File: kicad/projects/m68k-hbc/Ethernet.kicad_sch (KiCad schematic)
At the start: 19 parts, among them J17 RJ45_Amphenol_RJMG1BD3B8K1ANR, U29 RTL8019AS, Y7 20M

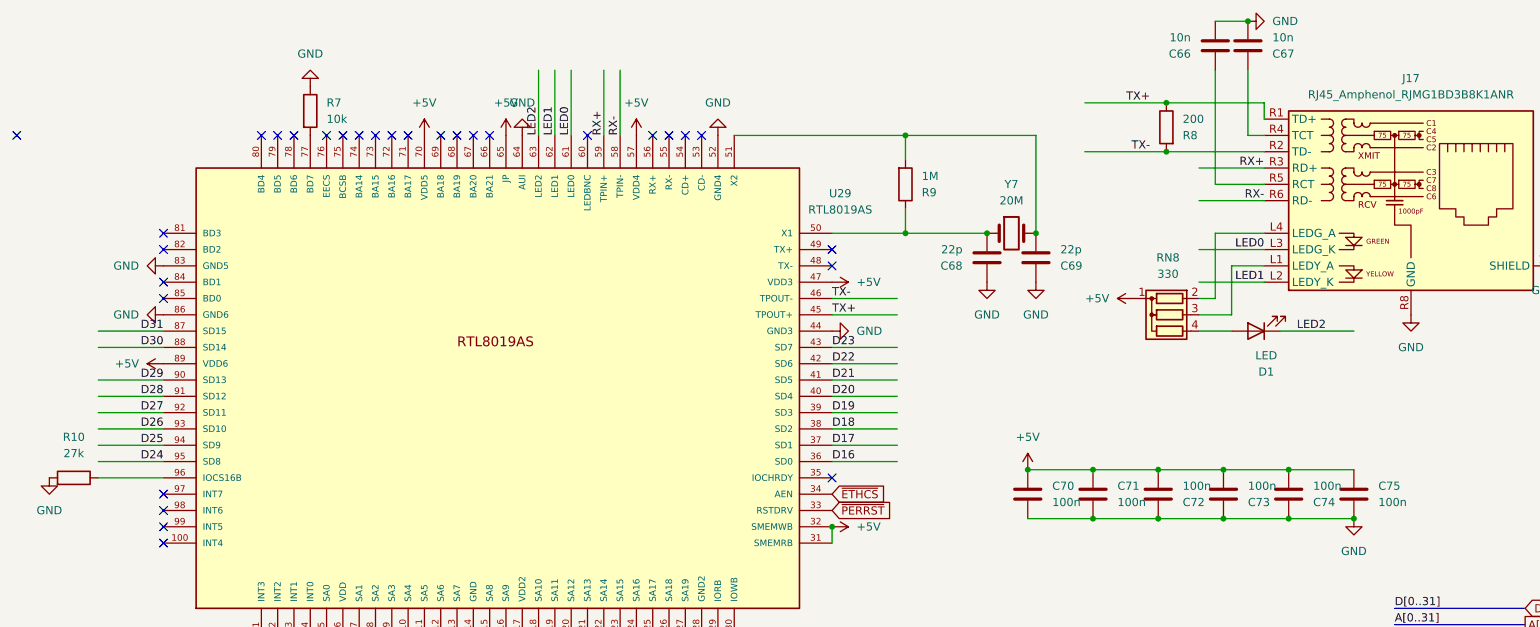
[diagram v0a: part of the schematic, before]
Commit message: Modified system architecture, New KiCad Project: Cache Memory Module(SIMM80)
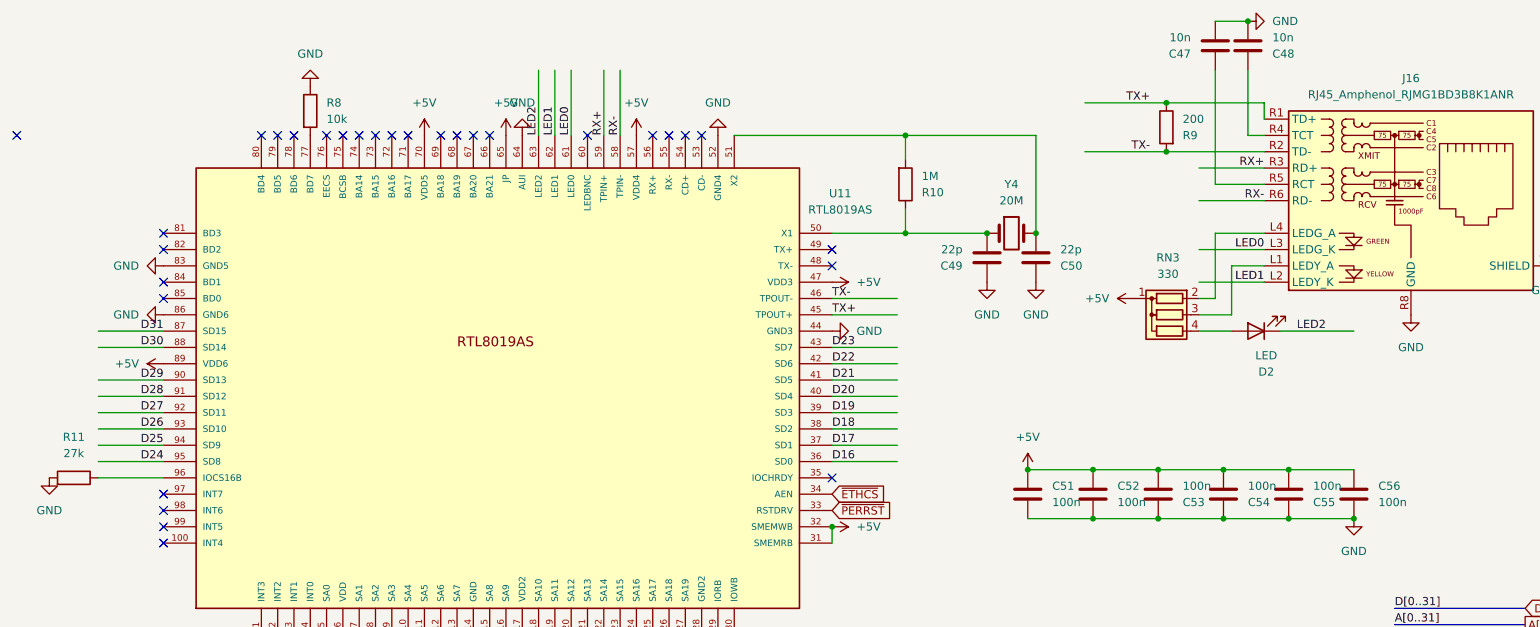
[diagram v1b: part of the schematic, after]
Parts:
- renumbered C66 to C47, C67 to C48, C68 to C49, C69 to C50, C70 to C51, C71 to C52, C72 to C53, C73 to C54, C74 to C55, C75 to C56, D1 to D2, J17 to J16, R9 to R10, R10 to R11, R7 to R8, R8 to R9, RN8 to RN3, U29 to U11, Y7 to Y4

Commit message: Some Updates
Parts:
- removed R11: 27k, Resistor_SMD:R_1206_3216Metric_Pad1.30x1.75mm_HandSolder, symbol Device:R
- removed R8: 10k, Resistor_SMD:R_1206_3216Metric_Pad1.30x1.75mm_HandSolder, symbol Device:R
- C67: renamed from C47; value 10n -> C; footprint Capacitor_SMD:C_1206_3216Metric_Pad1.33x1.80mm_HandSolder -> Capacitor_SMD:C_0603_1608Metric_Pad1.08x0.95mm_HandSolder
- C68: renamed from C48; value 10n -> C; footprint Capacitor_SMD:C_1206_3216Metric_Pad1.33x1.80mm_HandSolder -> Capacitor_SMD:C_0603_1608Metric_Pad1.08x0.95mm_HandSolder
- C69: renamed from C49; value 22p -> C; footprint Capacitor_SMD:C_1206_3216Metric_Pad1.33x1.80mm_HandSolder -> Capacitor_SMD:C_0603_1608Metric_Pad1.08x0.95mm_HandSolder
- C70: renamed from C50; value 22p -> C; footprint Capacitor_SMD:C_1206_3216Metric_Pad1.33x1.80mm_HandSolder -> Capacitor_SMD:C_0603_1608Metric_Pad1.08x0.95mm_HandSolder
- C71: renamed from C51; value 100n -> C; footprint Capacitor_SMD:C_1206_3216Metric_Pad1.33x1.80mm_HandSolder -> Capacitor_SMD:C_0603_1608Metric_Pad1.08x0.95mm_HandSolder
- C72: renamed from C52; value 100n -> C; footprint Capacitor_SMD:C_1206_3216Metric_Pad1.33x1.80mm_HandSolder -> Capacitor_SMD:C_0603_1608Metric_Pad1.08x0.95mm_HandSolder
- C73: renamed from C53; value 100n -> C; footprint Capacitor_SMD:C_1206_3216Metric_Pad1.33x1.80mm_HandSolder -> Capacitor_SMD:C_0603_1608Metric_Pad1.08x0.95mm_HandSolder
- C74: renamed from C54; value 100n -> C; footprint Capacitor_SMD:C_1206_3216Metric_Pad1.33x1.80mm_HandSolder -> Capacitor_SMD:C_0603_1608Metric_Pad1.08x0.95mm_HandSolder
- C75: renamed from C55; value 100n -> C; footprint Capacitor_SMD:C_1206_3216Metric_Pad1.33x1.80mm_HandSolder -> Capacitor_SMD:C_0603_1608Metric_Pad1.08x0.95mm_HandSolder
- C76: renamed from C56; value 100n -> C; footprint Capacitor_SMD:C_1206_3216Metric_Pad1.33x1.80mm_HandSolder -> Capacitor_SMD:C_0603_1608Metric_Pad1.08x0.95mm_HandSolder
- R6: renamed from R9; value 200 -> R; footprint Resistor_SMD:R_1206_3216Metric_Pad1.30x1.75mm_HandSolder -> Resistor_SMD:R_0603_1608Metric_Pad0.98x0.95mm_HandSolder
- R7: renamed from R10; value 1M -> R; footprint Resistor_SMD:R_1206_3216Metric_Pad1.30x1.75mm_HandSolder -> Resistor_SMD:R_0603_1608Metric_Pad0.98x0.95mm_HandSolder
- RN3: value 330 -> R_Network03
- Y3: renamed from Y4; value 20M -> Crystal
- renumbered D2 to D1, J16 to J14, U11 to U20
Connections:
- net +5V: no longer U20.15 (SA8), U20.16 (SA9), U20.31 (SMEMRB), U20.32 (SMEMWB)
- net GND: no longer U20.11 (SA5), U20.12 (SA6), U20.13 (SA7), U20.18 (SA10), U20.19 (SA11), U20.20 (SA12), U20.21 (SA13), U20.22 (SA14), U20.23 (SA15), U20.24 (SA16), U20.25 (SA17), U20.26 (SA18), U20.27 (SA19)
- net ISA_IRQ5: now reaches U20.1 (INT3)
- net ISA_IRQ10: now reaches U20.100 (INT4)
- net ISA_IRQ4: now reaches U20.2 (INT2)
- net ISA_IRQ3: now reaches U20.3 (INT1)
- net ISA_IORDY: now reaches U20.35 (IOCHRDY)
- net ISA_IRQ2: now reaches U20.4 (INT0)
- net ~{ISA_IOCS16}: now reaches U20.96 (IOCS16B)
- net ISA_IRQ15: now reaches U20.97 (INT7)
- net ISA_IRQ12: now reaches U20.98 (INT6)
- net ISA_IRQ11: now reaches U20.99 (INT5)
- net A1 renamed ISA_A0
- net A2 renamed ISA_A7
- net A3 renamed ISA_A6
- net A4 renamed ISA_A5
- net A5 renamed ISA_A4
- net D16 renamed ISA_D0
- net D17 renamed ISA_D1
- net D18 renamed ISA_D2
- net D19 renamed ISA_D3
- net D20 renamed ISA_D4
- net D21 renamed ISA_D5
- net D22 renamed ISA_D6
- net D23 renamed ISA_D7
- net D24 renamed ISA_D8
- net D25 renamed ISA_D9
- net D26 renamed ISA_D10
- net D27 renamed ISA_D11
- net D28 renamed ISA_D12
- net D29 renamed ISA_D13
- net D30 renamed ISA_D14
- net D31 renamed ISA_D15
- net ~{ETHCS} renamed ISA_AEN
- net ~{PERRST} renamed ~{RST_ETH}
- net ~{RD} renamed ~{ISA_IOR}
- net ~{WR} renamed ~{ISA_IOW}
- new net ISA_A1: U20.13 (SA7)
- new net ISA_A10: U20.18 (SA10)
- new net ISA_A11: U20.19 (SA11)
- new net ISA_A12: U20.20 (SA12)
- new net ISA_A13: U20.21 (SA13)
- new net ISA_A14: U20.22 (SA14)
- new net ISA_A15: U20.23 (SA15)
- new net ISA_A16: U20.24 (SA16)
- new net ISA_A17: U20.25 (SA17)
- new net ISA_A18: U20.26 (SA18)
- new net ISA_A19: U20.27 (SA19)
- new net ISA_A2: U20.12 (SA6)
- new net ISA_A3: U20.11 (SA5)
- new net ISA_A8: U20.15 (SA8)
- new net ISA_A9: U20.16 (SA9)
- new net ~{ISA_SMEMR}: U20.31 (SMEMRB)
- new net ~{ISA_SMEMW}: U20.32 (SMEMWB)
- no-connect marks 33 -> 7
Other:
- note added: "ISA Signals"

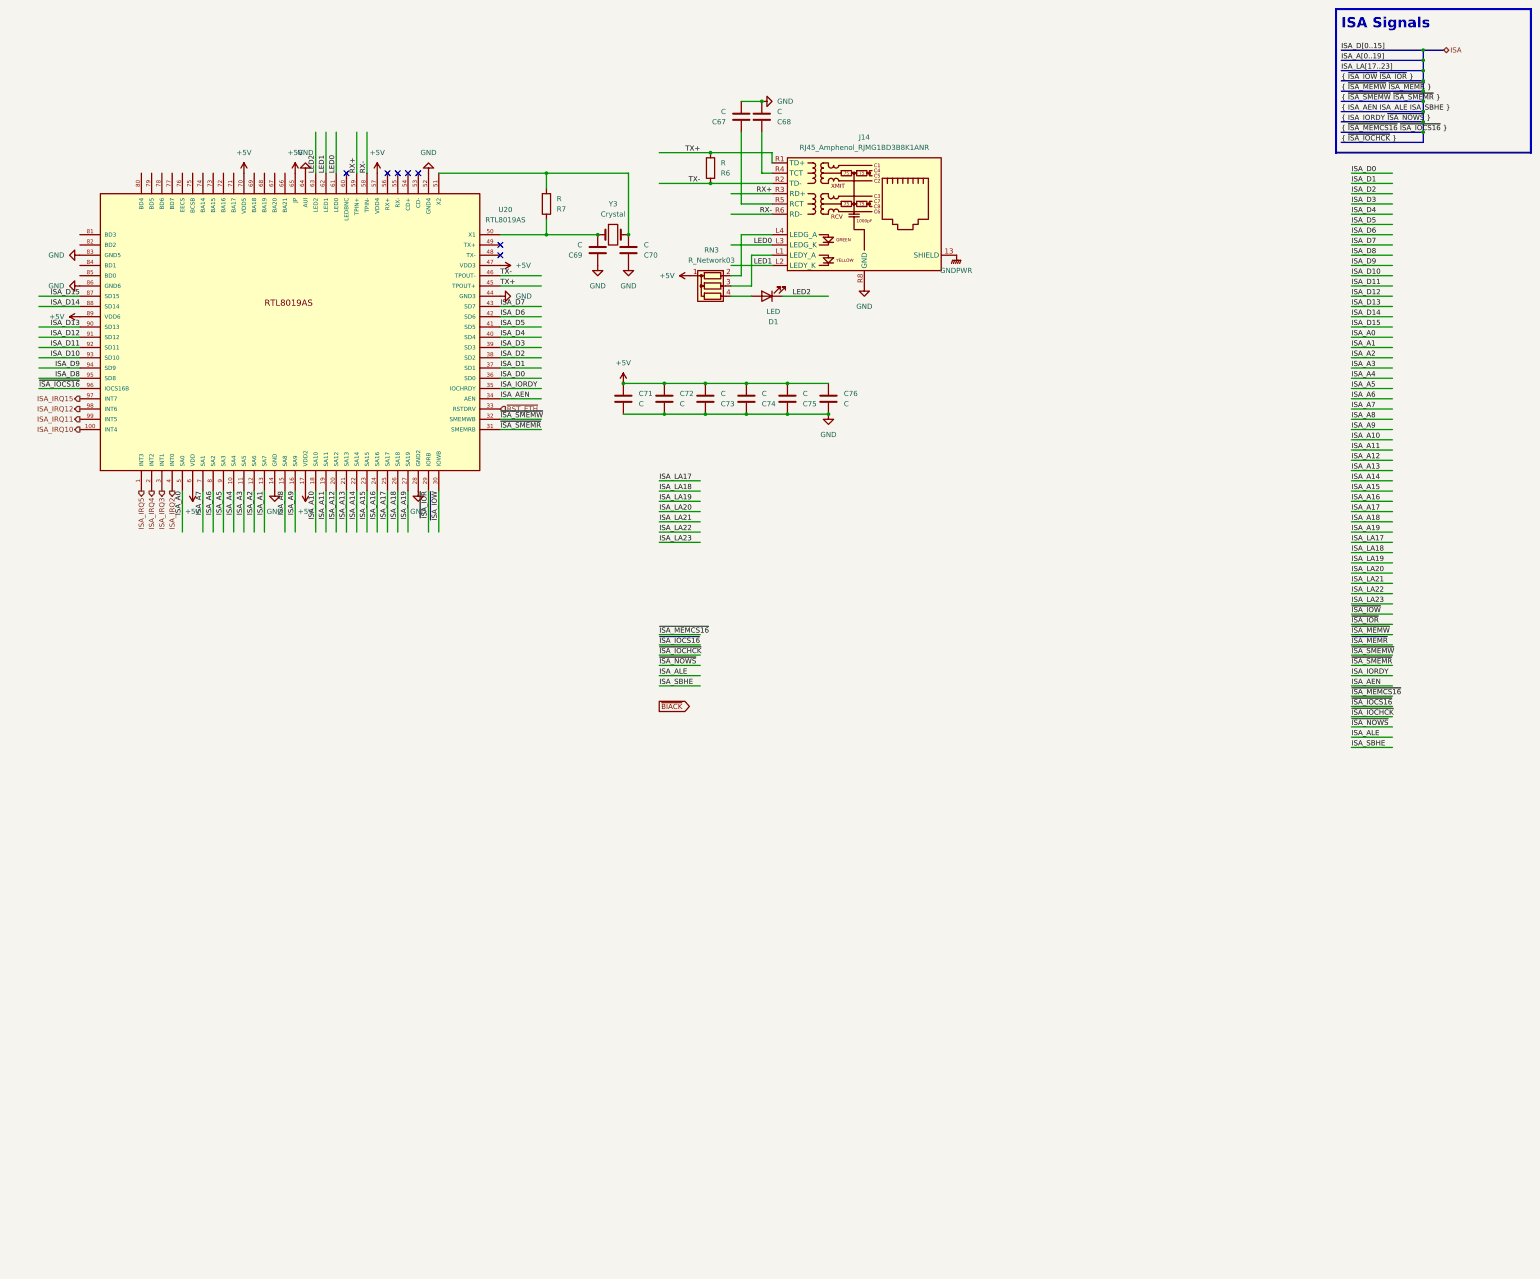
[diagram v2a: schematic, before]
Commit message: Large changes: EHBCSimpleEmu, kicad, fwcode, docs
This commit contains some large changes:
- Removed EHBCSimpleEmu (Moved to kms1212/llemu, kms1212/qemu)
- (likely) Removed fwcode; now it only boots and stops
- Modified documents
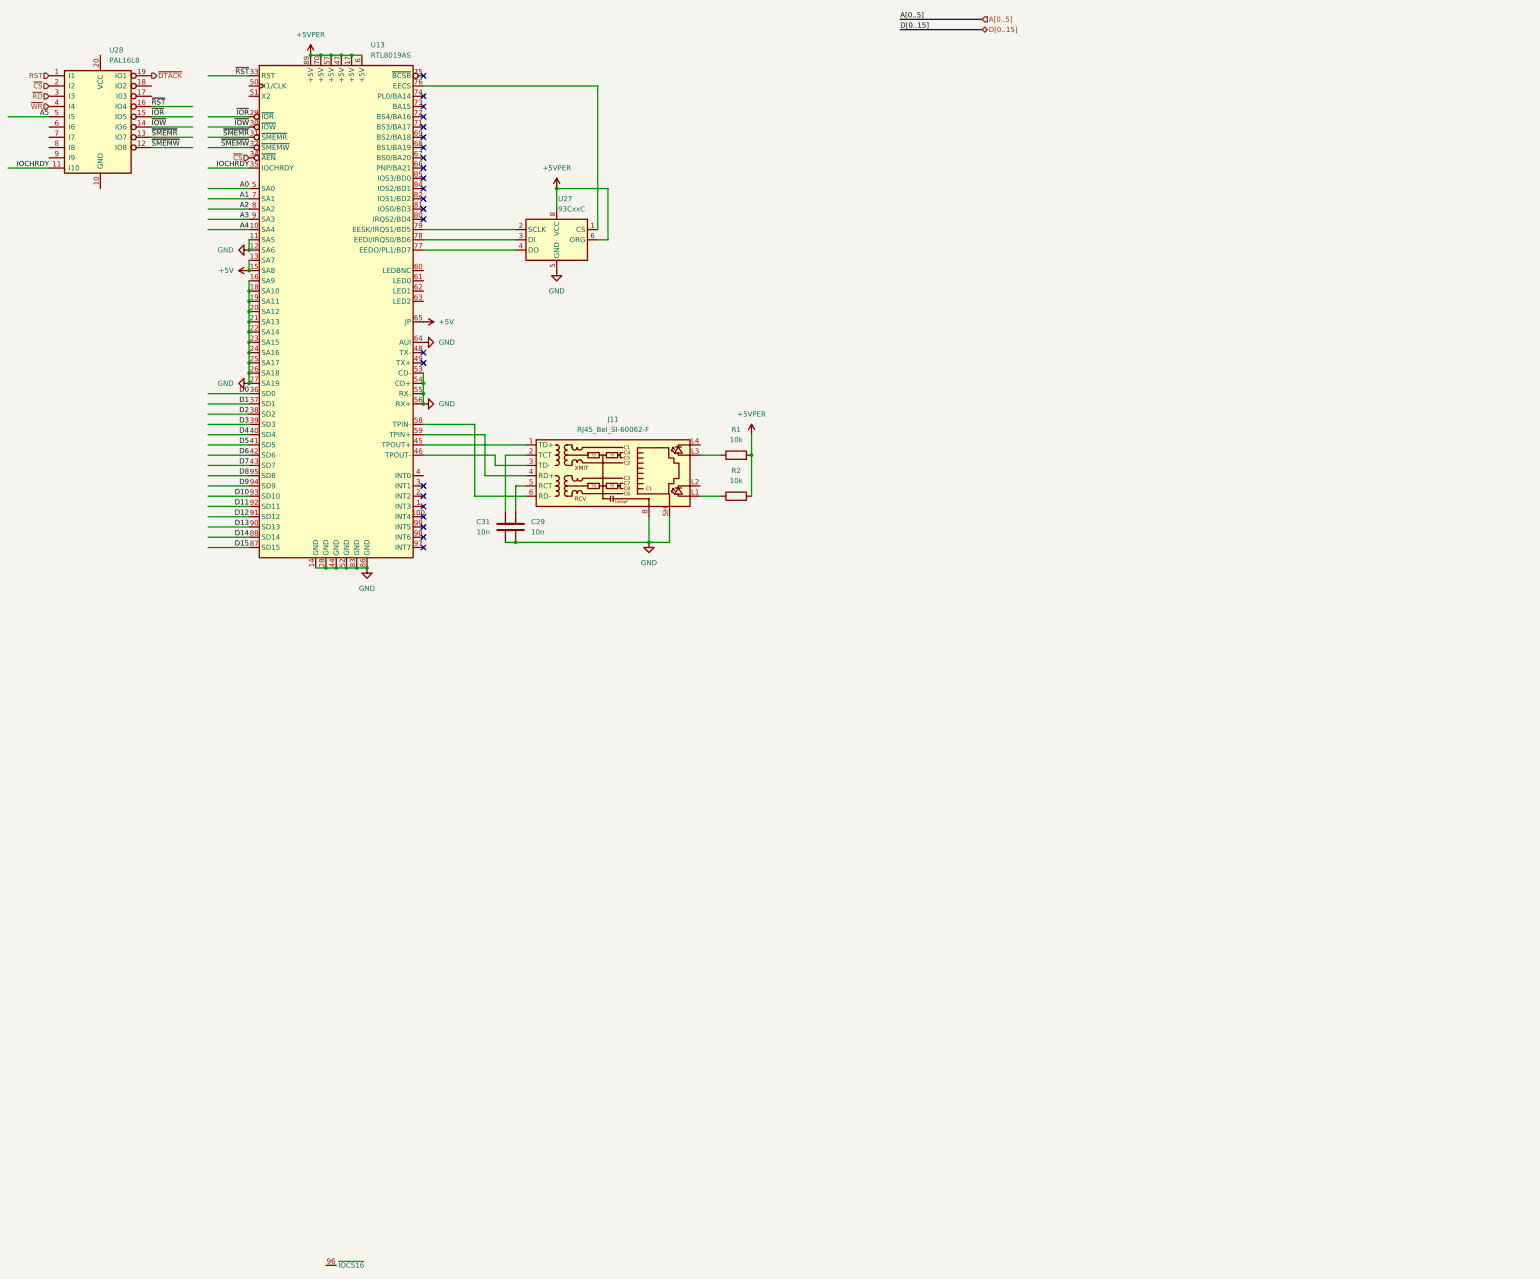
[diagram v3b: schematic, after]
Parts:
- removed C67, C68, C69, C70, C71, C72, C73, C74, C75, C76: C, Capacitor_SMD:C_0603_1608Metric_Pad1.08x0.95mm_HandSolder, symbol Device:C
- removed D1: LED, LED_THT:LED_D3.0mm, symbol Device:LED
- removed J14: RJ45_Amphenol_RJMG1BD3B8K1ANR, Connector_RJ:RJ45_Amphenol_RJMG1BD3B8K1ANR, symbol Connector:RJ45_Amphenol_RJMG1BD3B8K1ANR
- removed R6, R7: R, Resistor_SMD:R_0603_1608Metric_Pad0.98x0.95mm_HandSolder, symbol Device:R
- removed RN3: R_Network03, Resistor_THT:R_Array_SIP4, symbol Device:R_Network03
- removed U20: RTL8019AS, RTL8019AS:RTL8019AS, symbol RTL8019AS:RTL8019AS
- removed Y3: Crystal, Crystal:Crystal_HC52-6mm_Vertical, symbol Device:Crystal
- added C29, C31: 10n, symbol Device:C
- added J11: RJ45_Bel_SI-60062-F, Connector_RJ:RJ45_Bel_SI-60062-F, symbol Connector:RJ45_Bel_SI-60062-F
- added R1, R2: 10k, symbol Device:R
- added U13: RTL8019AS, RTL8019AS:RTL8019AS, symbol m68k-hbc-ic:RTL8019AS
- added U27: 93CxxC, Package_DIP:DIP-8_W7.62mm_Socket, symbol Memory_EEPROM:93CxxC
- added U28: PAL16L8, Package_DIP:DIP-20_W7.62mm_Socket, symbol Logic_Programmable:PAL16L8
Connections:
- net +5V: now also U13.13 (SA7), U13.15 (SA8), U13.65 (JP)
- net GND: now also C29.2, C31.2, J11.8, J11.SH, U13.11 (SA5), U13.12 (SA6), U13.14 (GND), U13.16 (SA9), U13.18 (SA10), U13.19 (SA11), U13.20 (SA12), U13.21 (SA13), U13.22 (SA14), U13.23 (SA15), U13.24 (SA16), U13.25 (SA17), U13.26 (SA18), U13.27 (SA19), U13.28 (GND), U13.44 (GND), U13.52 (GND), U13.53 (CD-), U13.54 (CD+), U13.55 (RX-), U13.56 (RX+), U13.64 (AUI), U13.83 (GND), U13.86 (GND), U27.5 (GND)
- new net: J11.1 (TD+), U13.45 (TPOUT+)
- new net: C31.1, J11.2 (TCT)
- new net: J11.3 (TD-), U13.46 (TPOUT-)
- new net: J11.4 (RD+), U13.59 (TPIN+)
- new net: C29.1, J11.5 (RCT)
- new net: J11.6 (RD-), U13.58 (TPIN-)
- new net: J11.L1, R2.1
- new net: J11.L3, R1.1
- new net: U13.76 (EECS), U27.1 (CS)
- new net: U13.77 (EEDO/PL1/BD7), U27.4 (DO)
- new net: U13.78 (EEDI/IRQS0/BD6), U27.3 (DI)
- new net: U13.79 (EESK/IRQS1/BD5), U27.2 (SCLK)
- new net +5VPER: R1.2, R2.2, U13.17 (+5V), U13.47 (+5V), U13.57 (+5V), U13.6 (+5V), U13.70 (+5V), U13.89 (+5V), U27.6 (ORG), U27.8 (VCC)
- new net A0: U13.5 (SA0)
- new net A1: U13.7 (SA1)
- new net A2: U13.8 (SA2)
- new net A3: U13.9 (SA3)
- new net A4: U13.10 (SA4)
- new net A5: U28.5 (I5)
- new net D0: U13.36 (SD0)
- new net D1: U13.37 (SD1)
- new net D10: U13.93 (SD10)
- new net D11: U13.92 (SD11)
- new net D12: U13.91 (SD12)
- new net D13: U13.90 (SD13)
- new net D14: U13.88 (SD14)
- new net D15: U13.87 (SD15)
- new net D2: U13.38 (SD2)
- new net D3: U13.39 (SD3)
- new net D4: U13.40 (SD4)
- new net D5: U13.41 (SD5)
- new net D6: U13.42 (SD6)
- new net D7: U13.43 (SD7)
- new net D8: U13.95 (SD8)
- new net D9: U13.94 (SD9)
- new net IOCHRDY: U13.35 (IOCHRDY), U28.11 (I10)
- new net RST: U28.1 (I1)
- new net ~{CS}: U13.34 (~{AEN}), U28.2 (I2)
- new net ~{DTACK}: U28.19 (IO1)
- new net ~{IOR}: U13.29 (~{IOR}), U28.15 (IO5)
- new net ~{IOW}: U13.30 (~{IOW}), U28.14 (IO6)
- new net ~{RD}: U28.3 (I3)
- new net ~{RST}: U13.33 (RST), U28.16 (IO4)
- new net ~{SMEMR}: U13.31 (~{SMEMR}), U28.13 (IO7)
- new net ~{SMEMW}: U13.32 (~{SMEMW}), U28.12 (IO8)
- new net ~{WR}: U28.4 (I4)
- no-connect marks 7 -> 23
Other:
- note removed: "ISA Signals"
